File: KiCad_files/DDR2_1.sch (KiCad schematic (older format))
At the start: 16 parts, among them J5 EDY4016A

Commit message: Cleanup + Update to KiCad 5.0 + DDR2
Updated to KiCad 5, which re-organized libraries, so corrected them to not need RASAC-rescue.lib.
Also cleaned up some stuff.
DDR4 has been removed and in place will be DDR2.
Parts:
- removed J5: EDY4016A, symbol EDY4016A
- C100, C89, C90, C91, C92, C93, C94, C95, C96, C97, C98, C99: symbol C_Small -> Device:C_Small
- R26, R27: symbol R -> Device:R
- R28: symbol R_Small -> Device:R_Small
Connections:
- net labels added: CAS_B, DDR2_A0, DDR2_A1, DDR2_A10, DDR2_A11, DDR2_A12, DDR2_A13, DDR2_A14, DDR2_A2, DDR2_A3, DDR2_A4, DDR2_A5, DDR2_A6, DDR2_A7, DDR2_A8, DDR2_A9, DDR2_BA0, DDR2_BA1, DDR2_BA2, DDR2_CKE, DDR2_CK_C, DDR2_CK_T, DDR2_CS_N, DDR2_DML, DDR2_DMU, DDR2_DQ0, DDR2_DQ1, DDR2_DQ10, DDR2_DQ11, DDR2_DQ12, DDR2_DQ13, DDR2_DQ14, DDR2_DQ15, DDR2_DQ2, DDR2_DQ3, DDR2_DQ4, DDR2_DQ5, DDR2_DQ6, DDR2_DQ7, DDR2_DQ8, DDR2_DQ9, DDR2_DQSL_C, DDR2_DQSL_T, DDR2_DQSU_C, DDR2_DQSU_T, DDR2_ODT, DDR2_RESET_N, RAS_B, WE_B
- net labels removed: DDR4_A0, DDR4_A1, DDR4_A10, DDR4_A11, DDR4_A12, DDR4_A13, DDR4_A14_WE_B, DDR4_A15_CAS_B, DDR4_A16_RAS_B, DDR4_A2, DDR4_A3, DDR4_A4, DDR4_A5, DDR4_A6, DDR4_A7, DDR4_A8, DDR4_A9, DDR4_ACT_N, DDR4_ALERT_N, DDR4_BA0, DDR4_BA1, DDR4_BG0, DDR4_CKE, DDR4_CK_C, DDR4_CK_T, DDR4_CS_N, DDR4_DM0, DDR4_DM1, DDR4_DQ0, DDR4_DQ1, DDR4_DQ10, DDR4_DQ11, DDR4_DQ12, DDR4_DQ13, DDR4_DQ14, DDR4_DQ15, DDR4_DQ2, DDR4_DQ3, DDR4_DQ4, DDR4_DQ5, DDR4_DQ6, DDR4_DQ7, DDR4_DQ8, DDR4_DQ9, DDR4_DQS0_C, DDR4_DQS0_T, DDR4_DQS1_C, DDR4_DQS1_T, DDR4_ODT, DDR4_PAR, DDR4_RESET_N, DDR4_TEN
- wire segments 79 -> 135

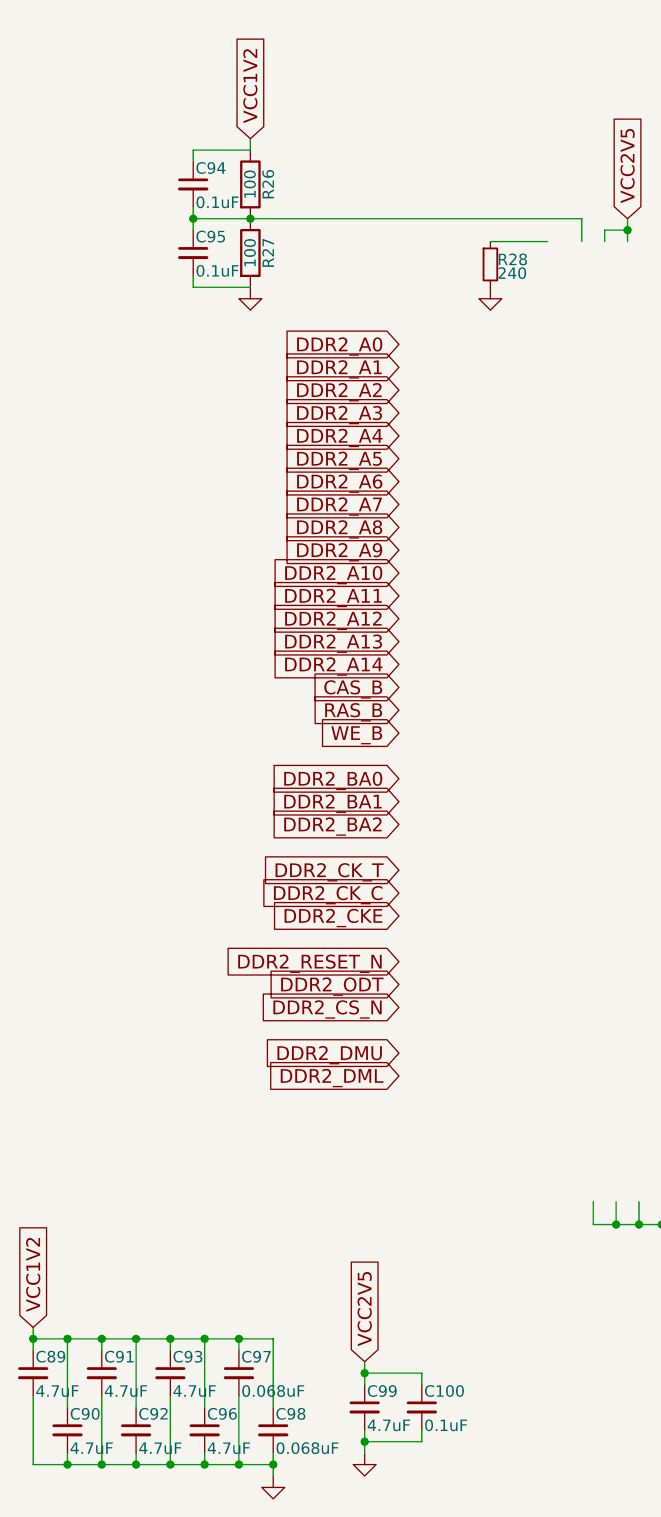
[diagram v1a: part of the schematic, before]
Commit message: Finished HDMI. Added I2C
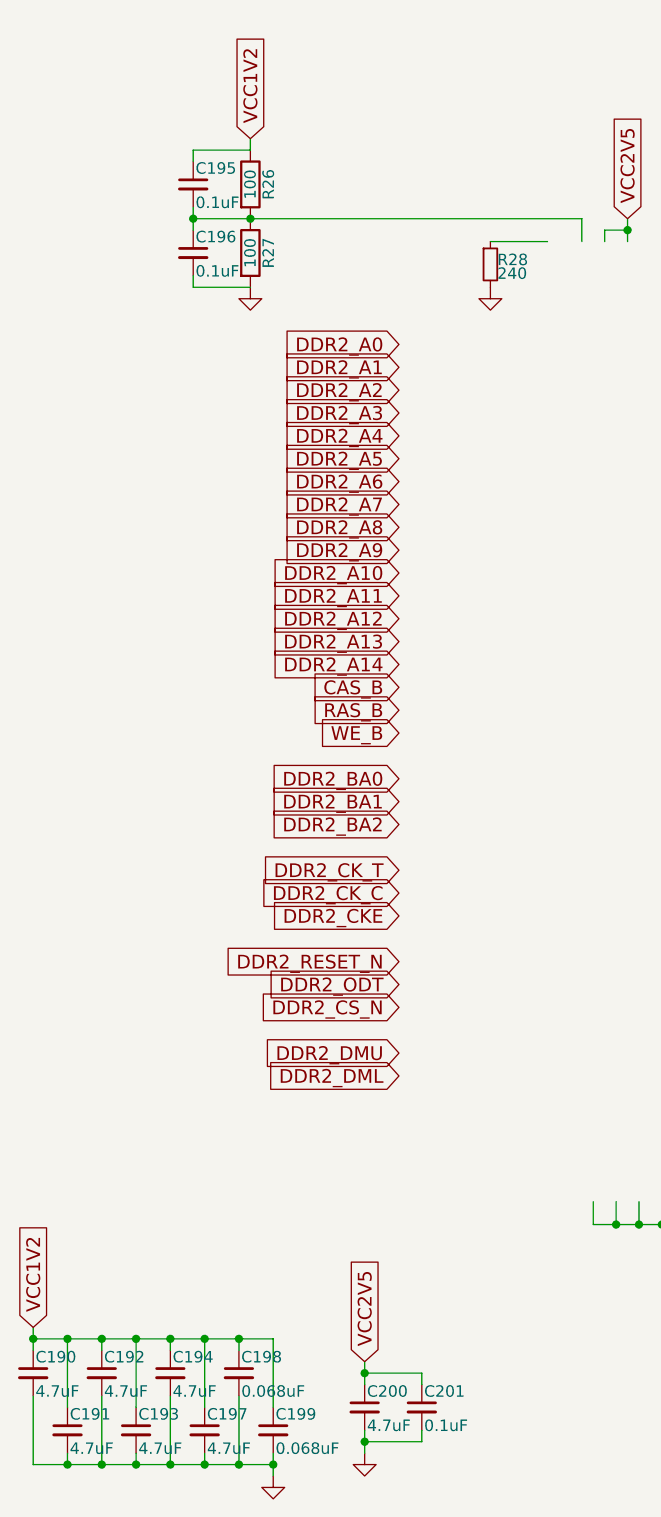
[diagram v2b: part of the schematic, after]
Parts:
- renumbered C89 to C190, C90 to C191, C91 to C192, C92 to C193, C93 to C194, C94 to C195, C95 to C196, C96 to C197, C97 to C198, C98 to C199, C99 to C200, C100 to C201
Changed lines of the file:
@@
 $EndComp
 $Comp
-L power:GND #PWR097
+L power:GND #PWR0103
 U 1 1 5C144778
 P 4350 1950
-F 0 "#PWR097" H 4350 1700 50  0001 C CNN
+F 0 "#PWR0103" H 4350 1700 50  0001 C CNN
 F 1 "GND" H 4350 1800 50  0001 C CNN
 F 2 "" H 4350 1950 50  0001 C CNN
@@
 $EndComp
 $Comp
-L power:GND #PWR098
+L power:GND #PWR0104
 U 1 1 5C144808
 P 5900 6150
-F 0 "#PWR098" H 5900 5900 50  0001 C CNN
+F 0 "#PWR0104" H 5900 5900 50  0001 C CNN
 F 1 "GND" H 5900 6000 50  0001 C CNN
 F 2 "" H 5900 6150 50  0001 C CNN
@@
 $EndComp
 $Comp
-L power:GND #PWR094
+L power:GND #PWR0100
 U 1 1 5C144B11
 P 3300 1950
-F 0 "#PWR094" H 3300 1700 50  0001 C CNN
+F 0 "#PWR0100" H 3300 1700 50  0001 C CNN
 F 1 "GND" H 3300 1800 50  0001 C CNN
 F 2 "" H 3300 1950 50  0001 C CNN
@@
 VCC1V2
 $Comp
-L Device:C_Small C95
+L Device:C_Small C196
 U 1 1 5C145216
 P 3050 1800
-F 0 "C95" H 3060 1870 50  0000 L CNN
+F 0 "C196" H 3060 1870 50  0000 L CNN
 F 1 "0.1uF" H 3060 1720 50  0000 L CNN
 F 2 "" H 3050 1800 50  0001 C CNN
@@
 $EndComp
 $Comp
-L Device:C_Small C94
+L Device:C_Small C195
 U 1 1 5C145289
 P 3050 1500
-F 0 "C94" H 3060 1570 50  0000 L CNN
+F 0 "C195" H 3060 1570 50  0000 L CNN
 F 1 "0.1uF" H 3060 1420 50  0000 L CNN
 F 2 "" H 3050 1500 50  0001 C CNN
@@
 VCC1V2
 $Comp
-L power:GND #PWR095
+L power:GND #PWR0101
 U 1 1 5C14848E
 P 3400 7150
-F 0 "#PWR095" H 3400 6900 50  0001 C CNN
+F 0 "#PWR0101" H 3400 6900 50  0001 C CNN
 F 1 "GND" H 3400 7000 50  0001 C CNN
 F 2 "" H 3400 7150 50  0001 C CNN
@@
 $EndComp
 $Comp
-L Device:C_Small C89
+L Device:C_Small C190
 U 1 1 5C1484C9
 P 2350 6700
-F 0 "C89" H 2360 6770 50  0000 L CNN
+F 0 "C190" H 2360 6770 50  0000 L CNN
 F 1 "4.7uF" H 2360 6620 50  0000 L CNN
 F 2 "" H 2350 6700 50  0001 C CNN
@@
 $EndComp
 $Comp
-L Device:C_Small C91
+L Device:C_Small C192
 U 1 1 5C14882E
 P 2650 6700
-F 0 "C91" H 2660 6770 50  0000 L CNN
+F 0 "C192" H 2660 6770 50  0000 L CNN
 F 1 "4.7uF" H 2660 6620 50  0000 L CNN
 F 2 "" H 2650 6700 50  0001 C CNN
@@
 $EndComp
 $Comp
-L Device:C_Small C93
+L Device:C_Small C194
 U 1 1 5C1488A8
 P 2950 6700
-F 0 "C93" H 2960 6770 50  0000 L CNN
+F 0 "C194" H 2960 6770 50  0000 L CNN
 F 1 "4.7uF" H 2960 6620 50  0000 L CNN
 F 2 "" H 2950 6700 50  0001 C CNN
@@
 $EndComp
 $Comp
-L Device:C_Small C97
+L Device:C_Small C198
 U 1 1 5C1488AE
 P 3250 6700
-F 0 "C97" H 3260 6770 50  0000 L CNN
+F 0 "C198" H 3260 6770 50  0000 L CNN
 F 1 "0.068uF" H 3260 6620 50  0000 L CNN
 F 2 "" H 3250 6700 50  0001 C CNN
@@
 $EndComp
 $Comp
-L Device:C_Small C90
+L Device:C_Small C191
 U 1 1 5C148AAE
 P 2500 6950
-F 0 "C90" H 2510 7020 50  0000 L CNN
+F 0 "C191" H 2510 7020 50  0000 L CNN
 F 1 "4.7uF" H 2510 6870 50  0000 L CNN
 F 2 "" H 2500 6950 50  0001 C CNN
@@
 $EndComp
 $Comp
-L Device:C_Small C92
+L Device:C_Small C193
 U 1 1 5C148AB4
 P 2800 6950
-F 0 "C92" H 2810 7020 50  0000 L CNN
+F 0 "C193" H 2810 7020 50  0000 L CNN
 F 1 "4.7uF" H 2810 6870 50  0000 L CNN
 F 2 "" H 2800 6950 50  0001 C CNN
@@
 $EndComp
 $Comp
-L Device:C_Small C96
+L Device:C_Small C197
 U 1 1 5C148ABA
 P 3100 6950
-F 0 "C96" H 3110 7020 50  0000 L CNN
+F 0 "C197" H 3110 7020 50  0000 L CNN
 F 1 "4.7uF" H 3110 6870 50  0000 L CNN
 F 2 "" H 3100 6950 50  0001 C CNN
@@
 $EndComp
 $Comp
-L Device:C_Small C98
+L Device:C_Small C199
 U 1 1 5C148AC0
 P 3400 6950
-F 0 "C98" H 3410 7020 50  0000 L CNN
+F 0 "C199" H 3410 7020 50  0000 L CNN
 F 1 "0.068uF" H 3410 6870 50  0000 L CNN
 F 2 "" H 3400 6950 50  0001 C CNN
@@
 Connection ~ 3250 7100
 $Comp
-L Device:C_Small C99
+L Device:C_Small C200
 U 1 1 5C149C6F
 P 3800 6850
-F 0 "C99" H 3810 6920 50  0000 L CNN
+F 0 "C200" H 3810 6920 50  0000 L CNN
 F 1 "4.7uF" H 3810 6770 50  0000 L CNN
 F 2 "" H 3800 6850 50  0001 C CNN
@@
 $EndComp
 $Comp
-L power:GND #PWR096
+L power:GND #PWR0102
 U 1 1 5C149CC6
 P 3800 7050
-F 0 "#PWR096" H 3800 6800 50  0001 C CNN
+F 0 "#PWR0102" H 3800 6800 50  0001 C CNN
 F 1 "GND" H 3800 6900 50  0001 C CNN
 F 2 "" H 3800 7050 50  0001 C CNN
@@
 $EndComp
 $Comp
-L Device:C_Small C100
+L Device:C_Small C201
 U 1 1 5C149D49
 P 4050 6850
-F 0 "C100" H 4060 6920 50  0000 L CNN
+F 0 "C201" H 4060 6920 50  0000 L CNN
 F 1 "0.1uF" H 4060 6770 50  0000 L CNN
 F 2 "" H 4050 6850 50  0001 C CNN

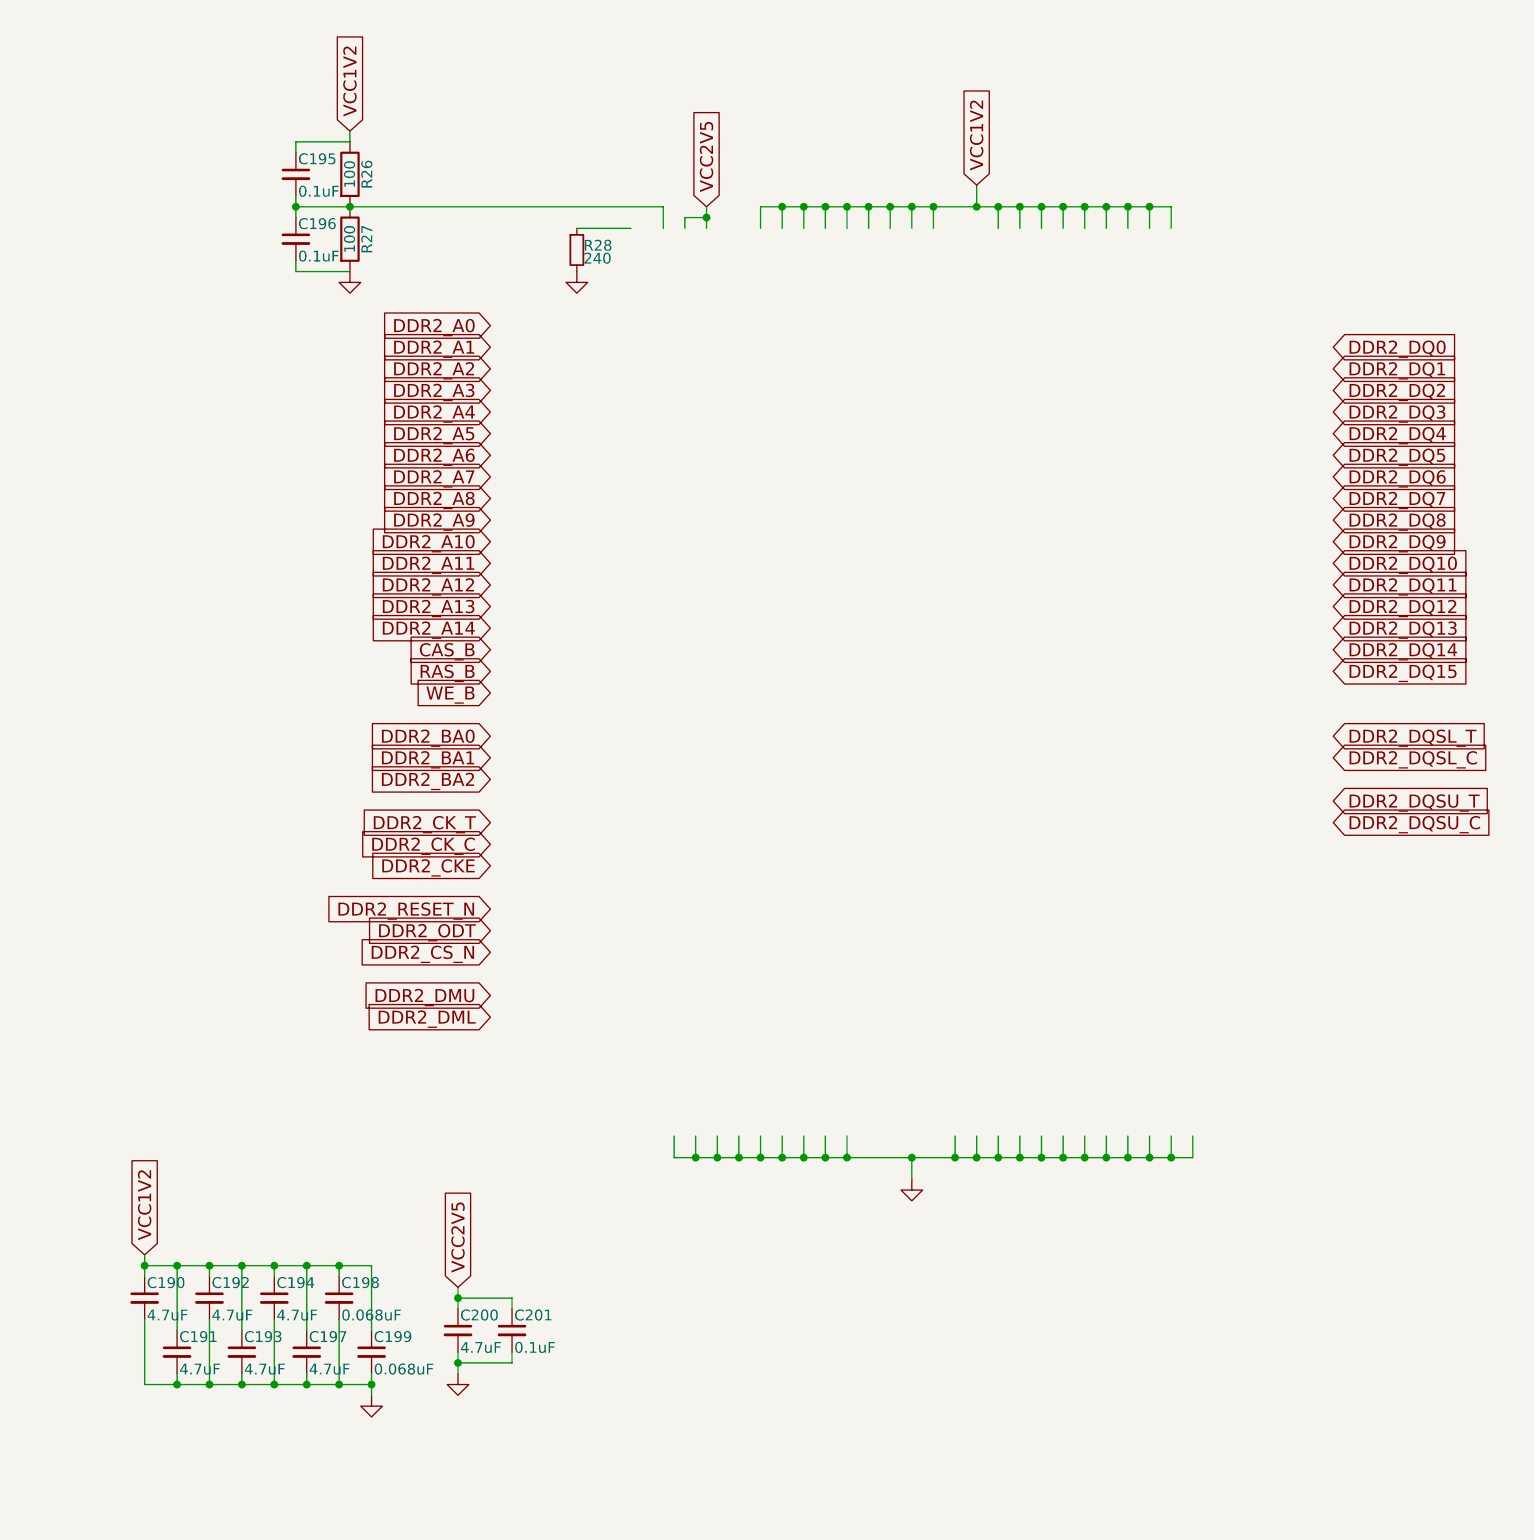
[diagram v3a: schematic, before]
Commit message: Cleanup for DRC and HDMI. HDMI and DDR2 looks good
DRC returns 5 errors with POWEROUTPUT-POWEROUTPUT set as good.
3 of them come from 3V3 since it's being driven from a MOSFET.
1 of them from VCC5V0 not yet supplied.
1 of them from USB_VBUS not set as output.
TODO:
5V supply for HDMI
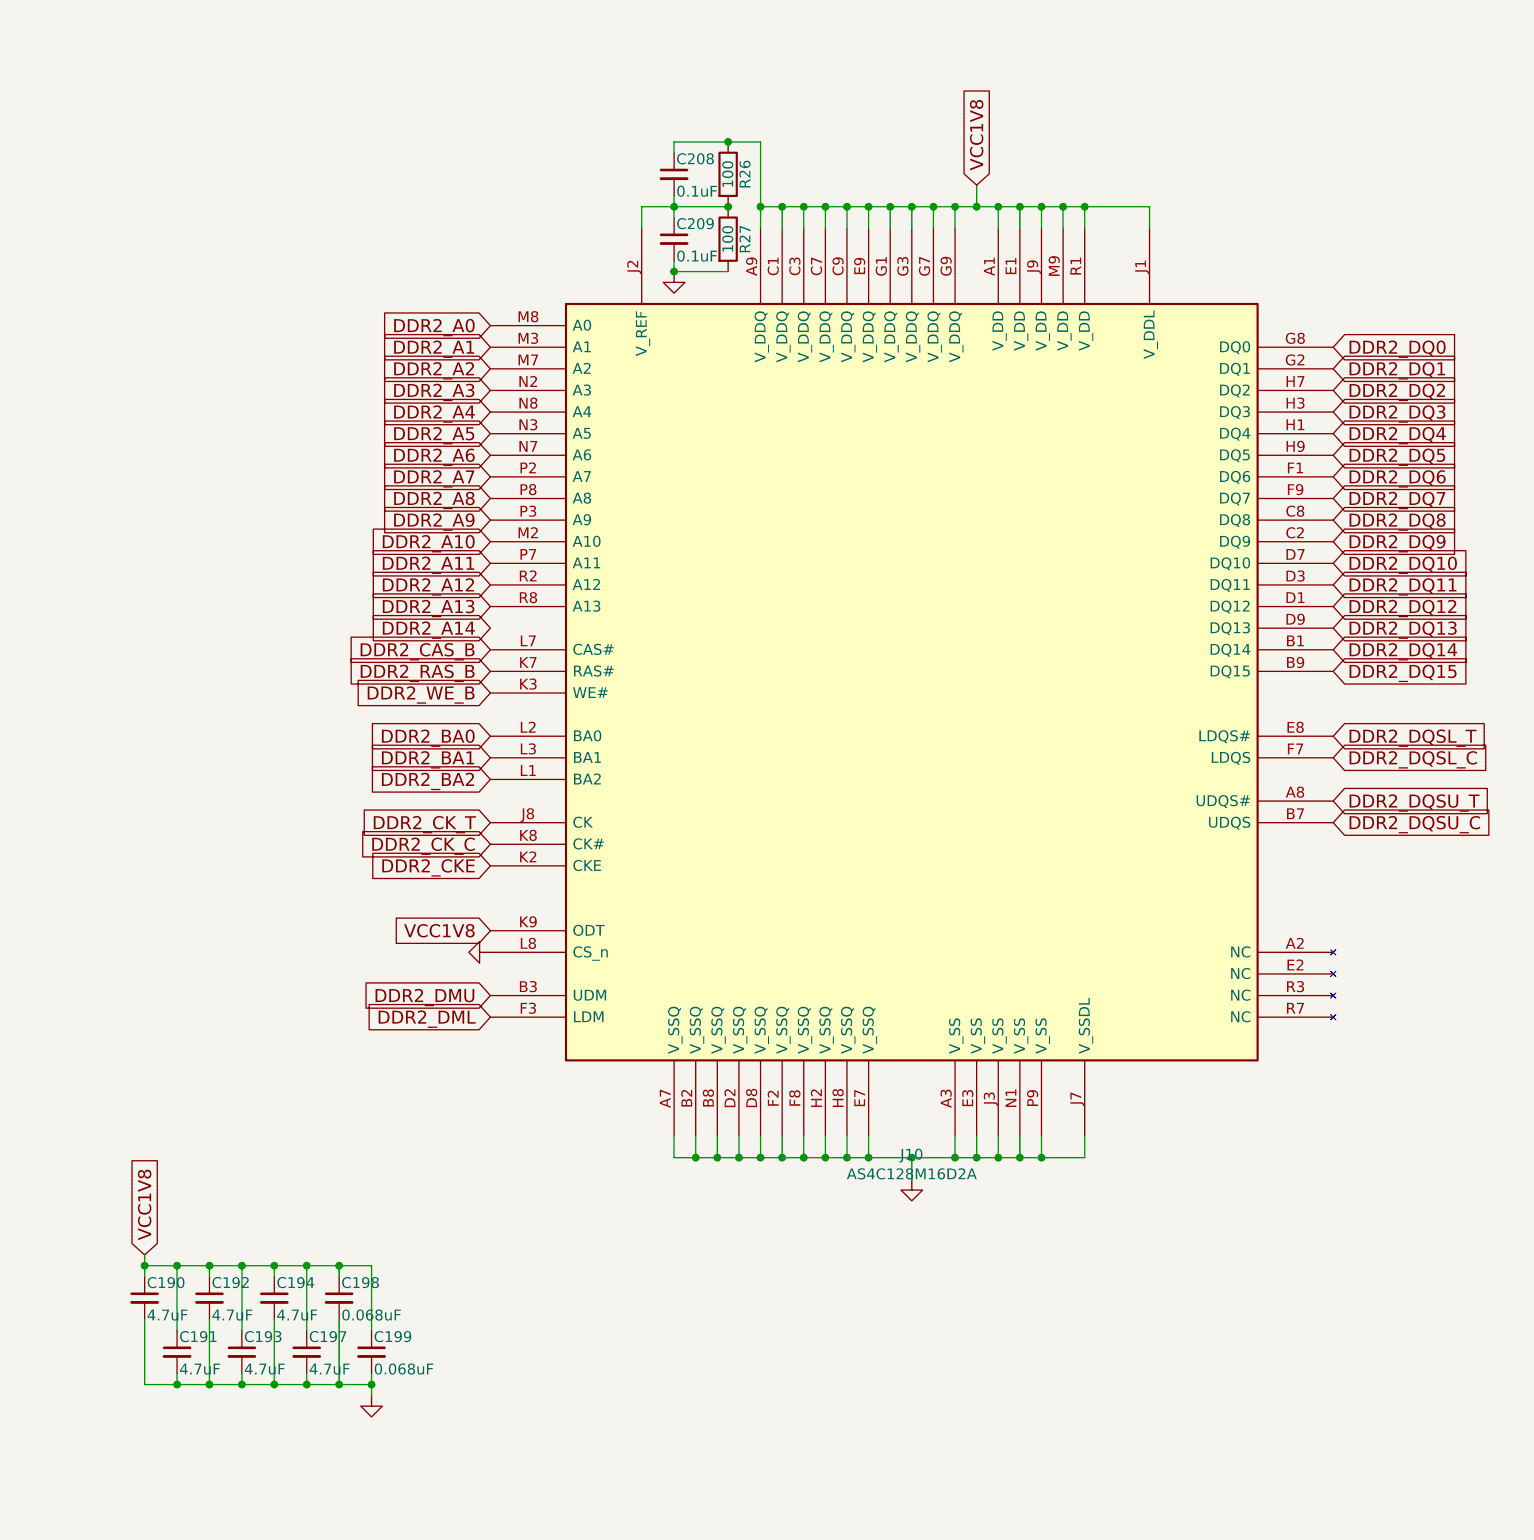
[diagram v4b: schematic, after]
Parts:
- removed C195, C196, C201: 0.1uF, symbol Device:C_Small
- removed C200: 4.7uF, symbol Device:C_Small
- removed R28: 240, symbol Device:R_Small
- added C208, C209: 0.1uF, symbol Device:C_Small
- added J10: AS4C128M16D2A, symbol custom:AS4C128M16D2A
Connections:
- net labels added: DDR2_CAS_B, DDR2_RAS_B, DDR2_WE_B, VCC1V8
- net labels removed: CAS_B, DDR2_CS_N, DDR2_ODT, DDR2_RESET_N, RAS_B, VCC1V2, VCC2V5, WE_B
- wire segments 135 -> 109
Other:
- moved on the sheet: R26, R27
